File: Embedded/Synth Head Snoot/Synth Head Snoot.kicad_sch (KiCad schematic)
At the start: 0 parts

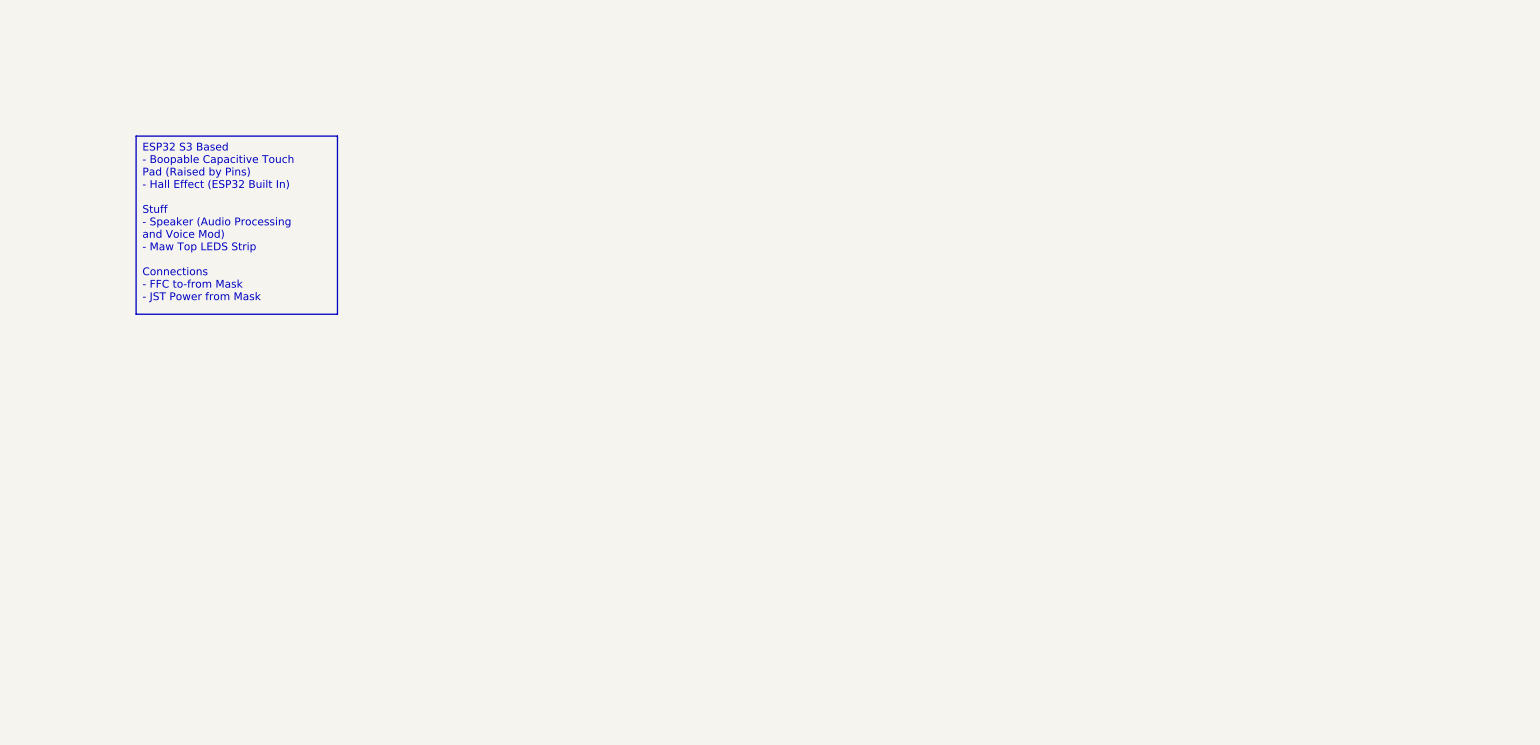
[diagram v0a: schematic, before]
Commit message: Majority of the pins for the Mask Board & Snoot Added
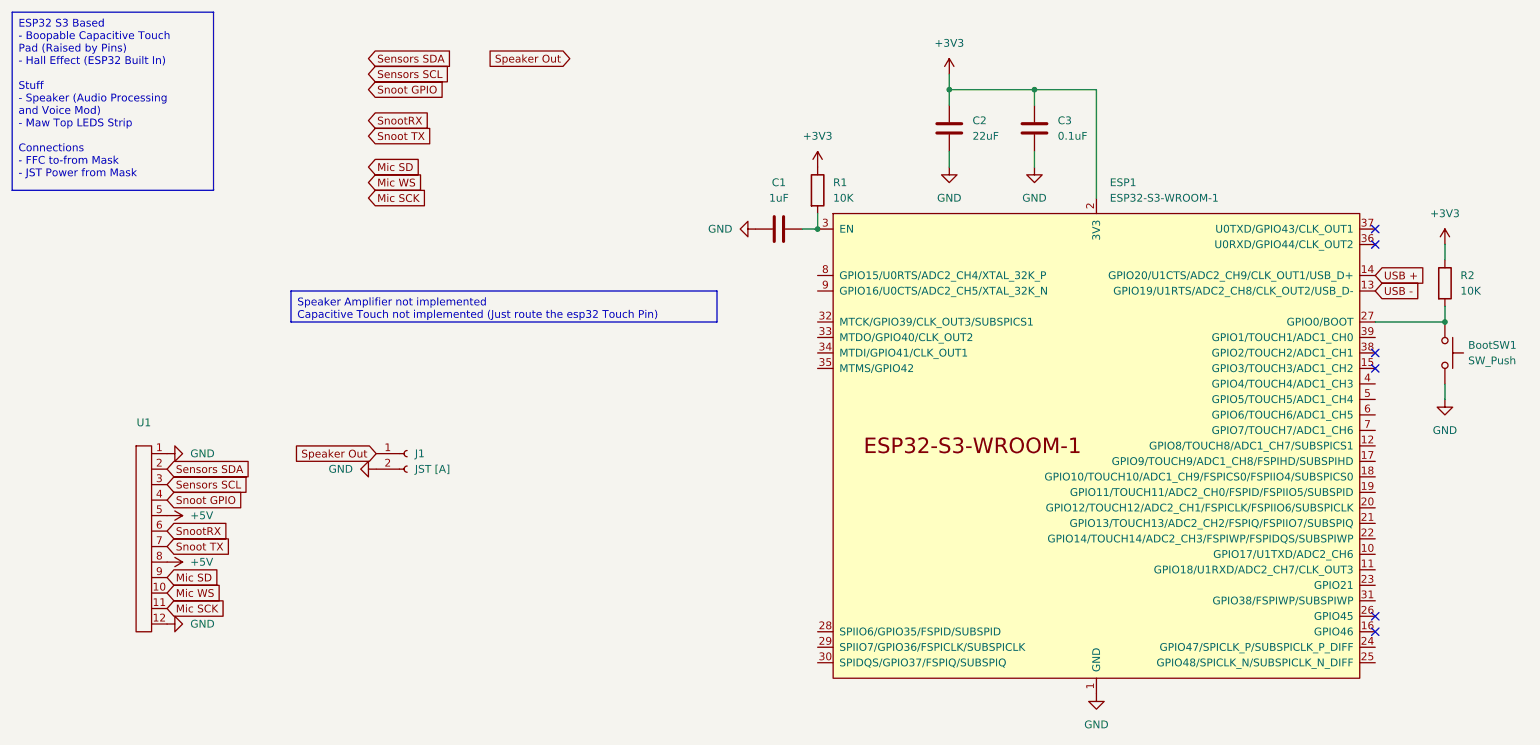
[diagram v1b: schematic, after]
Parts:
- added BootSW1: SW_Push, Button-R-667843:Button-R-667843, symbol Switch:SW_Push
- added C1: 1uF, Capacitor_SMD:C_0603_1608Metric, symbol Device:C
- added C2: 22uF, Capacitor_SMD:C_0603_1608Metric_Pad1.08x0.95mm_HandSolder, symbol Device:C
- added C3: 0.1uF, Capacitor_SMD:C_0603_1608Metric, symbol Device:C
- added ESP1: ESP32-S3-WROOM-1, PCM_Espressif:ESP32-S3-WROOM-1U, symbol PCM_Espressif:ESP32-S3-WROOM-1
- added J1: JST [A], symbol Connector:Conn_01x02_Socket
- added R1, R2: 10K, Resistor_SMD:R_0603_1608Metric, symbol Device:R
- added U1: ~, symbol FCC_Connector:FFC_12P
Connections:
- new net: C1.2, ESP1.3 (EN), R1.2
- new net: BootSW1.1, ESP1.27 (GPIO0/BOOT), R2.2
- new net +3V3: C2.1, C3.1, ESP1.2 (3V3), R1.1, R2.1
- new net +5V: U1.5, U1.8
- new net GND: BootSW1.2, C1.1, C2.2, C3.2, ESP1.1 (GND), ESP1.40 (GND), ESP1.41 (GND), J1.2 (Pin_2), U1.1, U1.12
- new net Mic SCK: U1.11
- new net Mic SD: U1.9
- new net Mic WS: U1.10
- new net Sensors SCL: U1.3
- new net Sensors SDA: U1.2
- new net Snoot GPIO: U1.4
- new net Snoot TX: U1.7
- new net SnootRX: U1.6
- new net Speaker Out: J1.1 (Pin_1)
- new net USB +: ESP1.14 (GPIO20/U1CTS/ADC2_CH9/CLK_OUT1/USB_D+)
- new net USB -: ESP1.13 (GPIO19/U1RTS/ADC2_CH8/CLK_OUT2/USB_D-)
- no-connect marks 0 -> 6

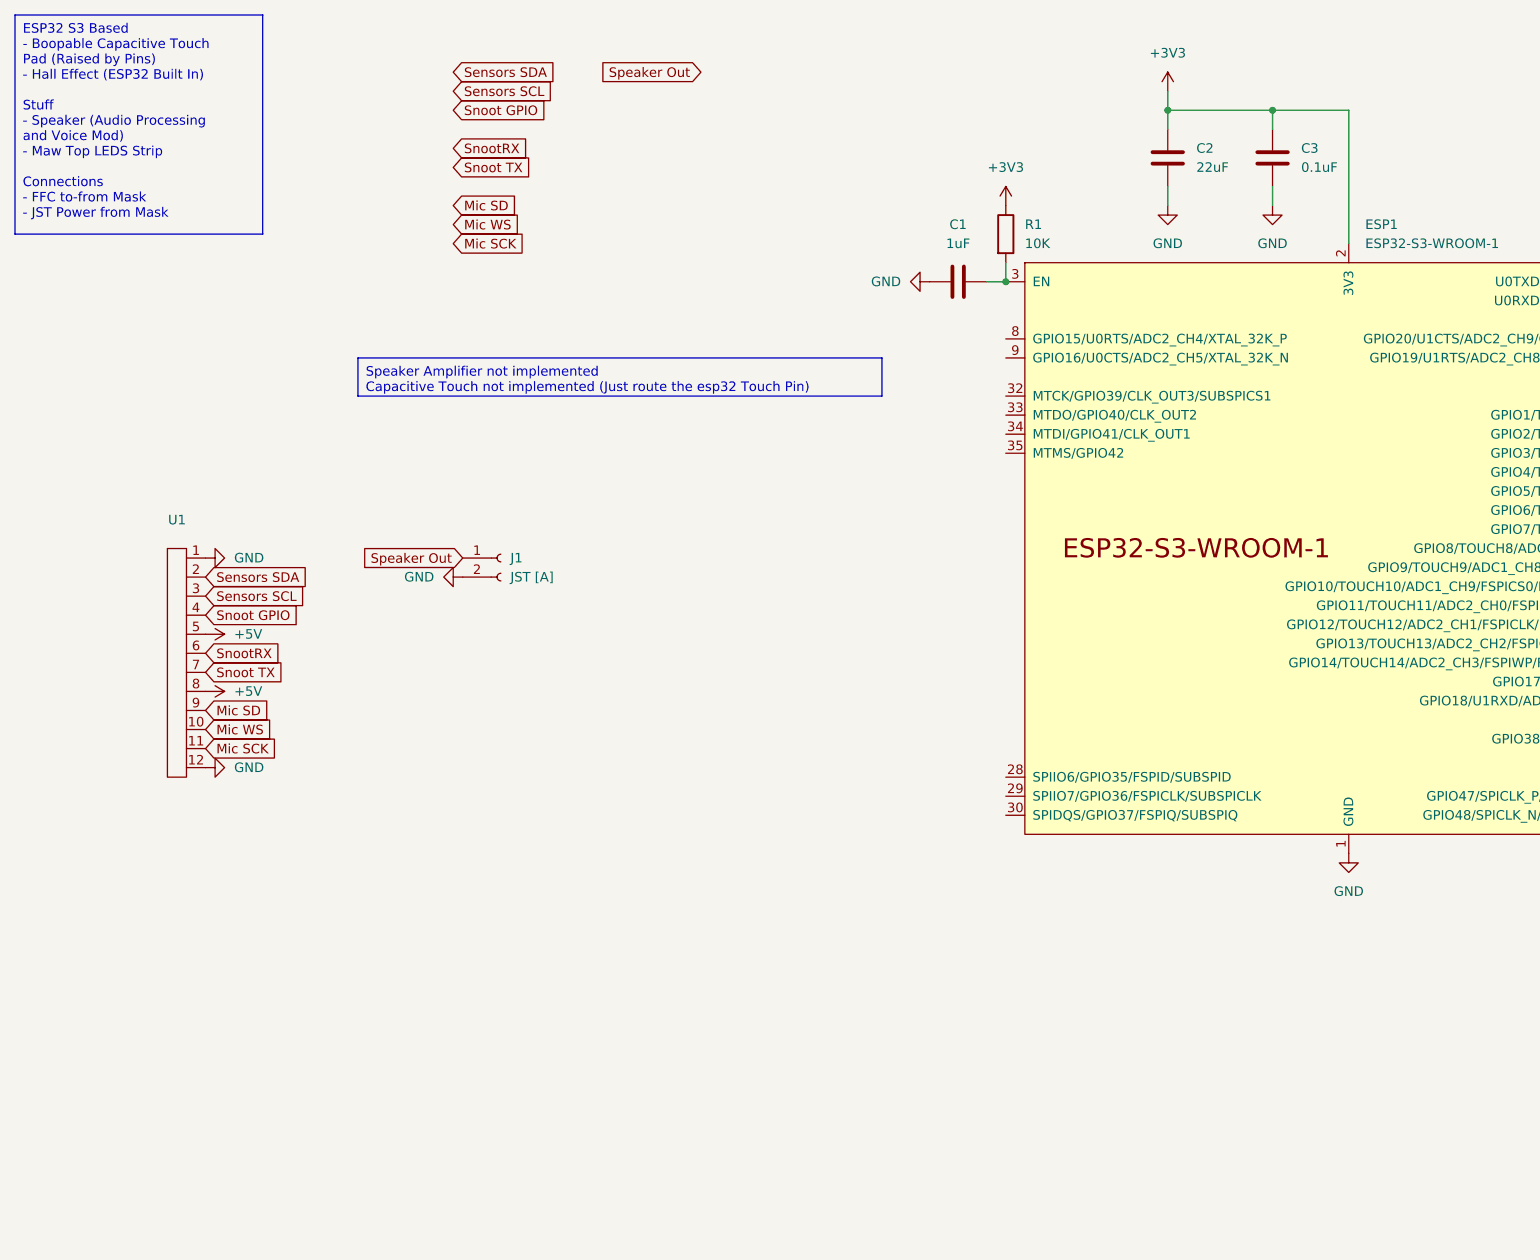
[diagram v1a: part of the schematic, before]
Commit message: Added Speaker, Power & USB C to Snoot Board
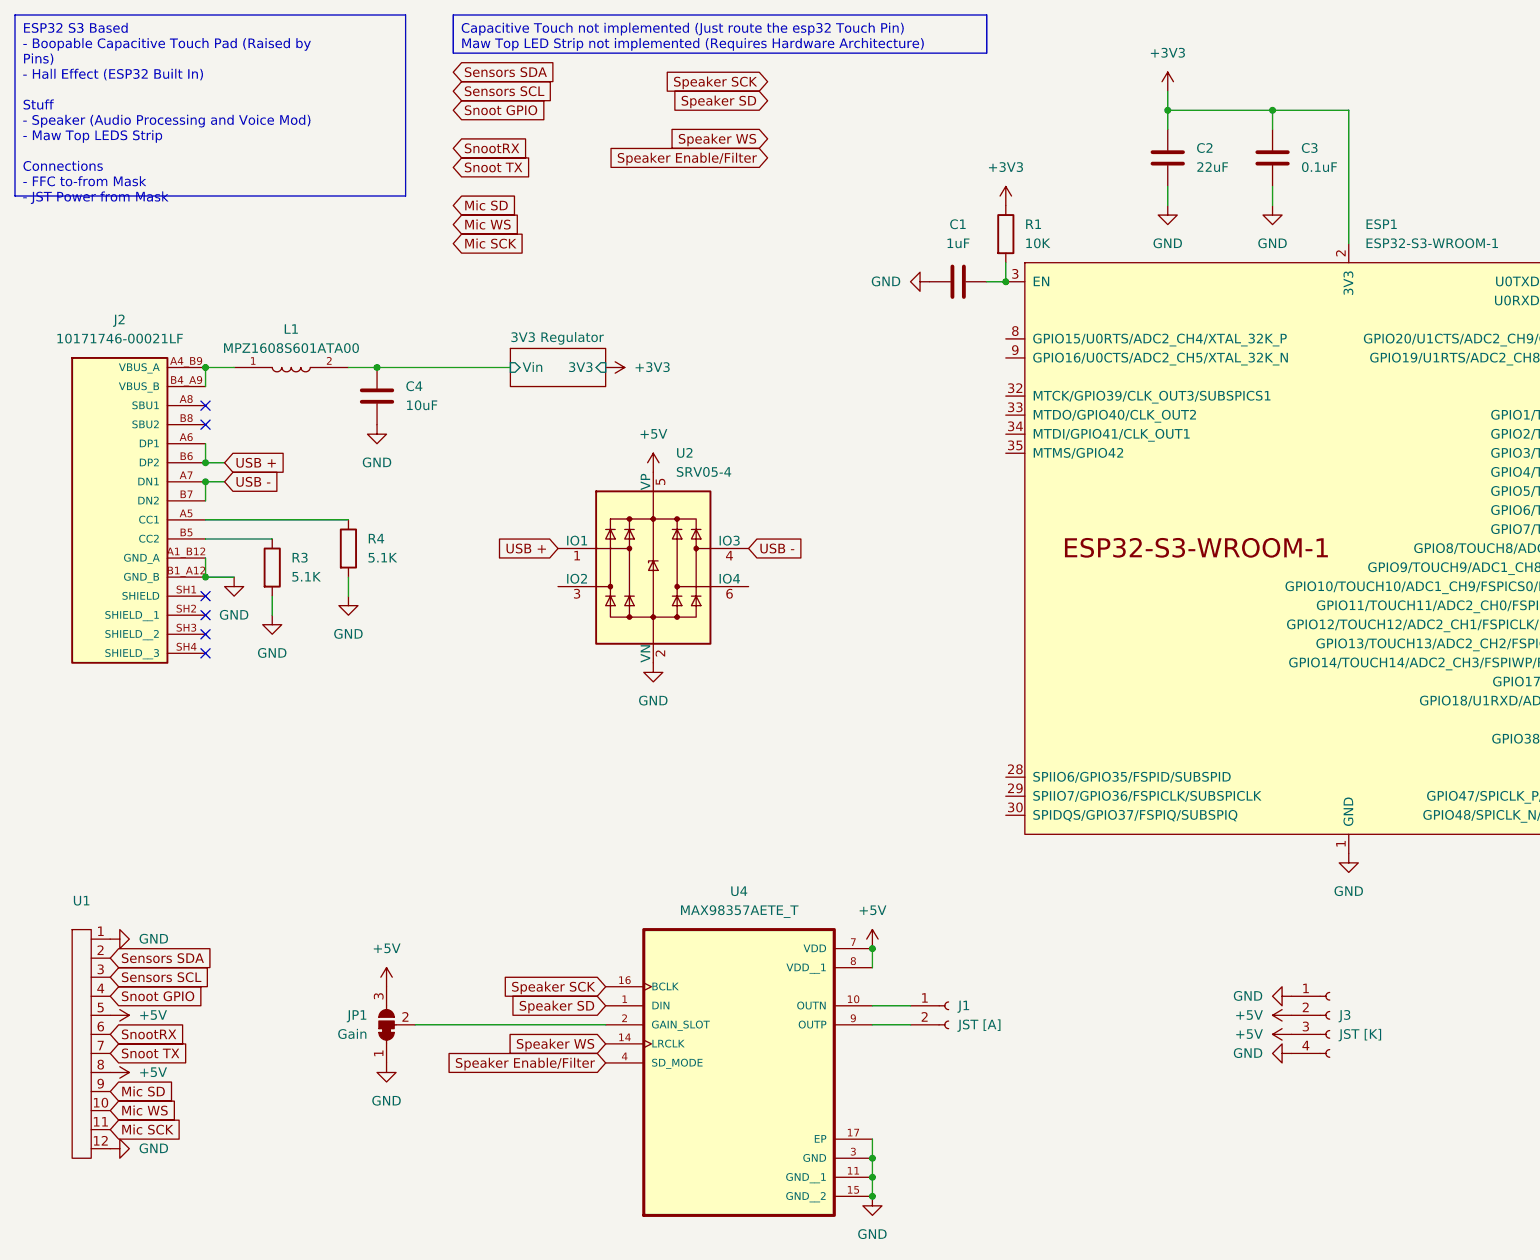
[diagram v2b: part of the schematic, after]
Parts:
- added C4: 10uF, Capacitor_SMD:C_0603_1608Metric, symbol Device:C
- added J2: 10171746-00021LF, USBC_10171746_00021LF:AMPHENOL_10171746-00021LF, symbol USBC_10171746_00021LF:10171746-00021LF
- added J3: JST [K], symbol Connector:Conn_01x04_Socket
- added JP1: Gain, symbol Jumper:SolderJumper_3_Bridged12
- added L1: MPZ1608S601ATA00, Ferrite_Bead_MPZ1608S601ATA00:INDC1608X95N, symbol Ferrite_Bead_MPZ1608S601ATA00:MPZ1608S601ATA00
- added R3, R4: 5.1K, Resistor_SMD:R_0603_1608Metric, symbol Device:R
- added U2: SRV05-4, Package_TO_SOT_SMD:SOT-23-6, symbol Power_Protection:SRV05-4
- added U4: MAX98357AETE_T, MAX98357AETE_T:QFN50P300X300X80-17N, symbol I2S_Audio_MAX98357A:MAX98357AETE_T
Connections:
- net +5V: now also J3.2 (Pin_2), J3.3 (Pin_3), JP1.3 (B), U2.5 (VP), U4.7 (VDD), U4.8 (VDD__1)
- net GND: now also C4.2, J2.A1_B12 (GND_A), J2.B1_A12 (GND_B), J3.1 (Pin_1), J3.4 (Pin_4), JP1.1 (A), R3.2, R4.2, U2.2 (VN), U4.11 (GND__1), U4.15 (GND__2), U4.17 (EP), U4.3 (GND); no longer J1.2 (Pin_2)
- net USB +: now also J2.A6 (DP1), J2.B6 (DP2), U2.1 (IO1)
- net USB -: now also J2.A7 (DN1), J2.B7 (DN2), U2.4 (IO3)
- net Speaker Out: no longer names the net of J1.1 (Pin_1)
- net Speaker Out: now also U4.10 (OUTN)
- new net: J1.2 (Pin_2), U4.9 (OUTP)
- new net: JP1.2 (C), U4.2 (GAIN_SLOT)
- new net: J2.B5 (CC2), R3.1
- new net: J2.A4_B9 (VBUS_A), J2.B4_A9 (VBUS_B), L1.1
- new net: J2.A5 (CC1), R4.1
- new net 3V3 Regulator/Vin: C4.1, L1.2
- new net Speaker Enable/Filter: U4.4 (SD_MODE)
- new net Speaker SCK: U4.16 (BCLK)
- new net Speaker SD: U4.1 (DIN)
- new net Speaker WS: U4.14 (LRCLK)
- no-connect marks 6 -> 12
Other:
- added sheet 3V3 Regulator (3V3 Reg.kicad_sch)
- moved on the sheet: J1, U1

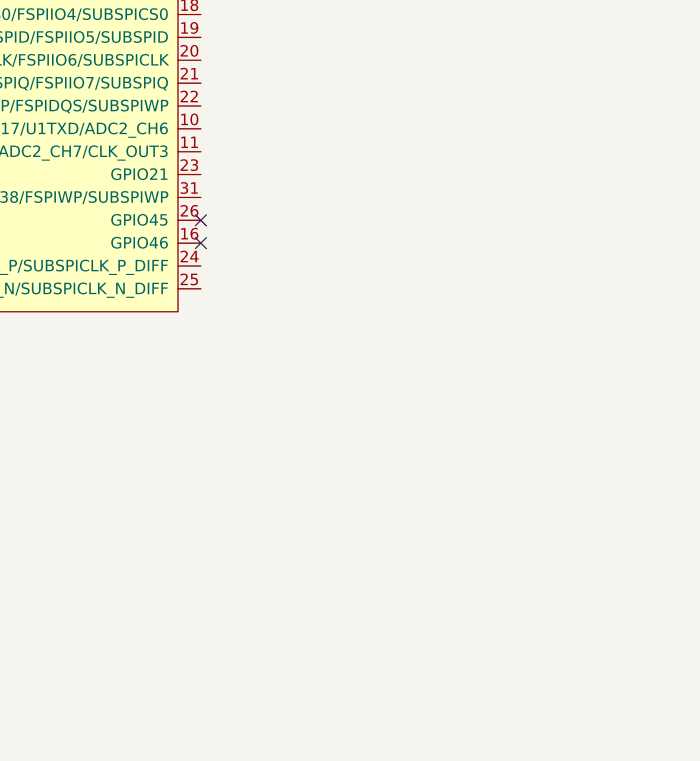
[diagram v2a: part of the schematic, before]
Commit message: Nearly completed Mask Board
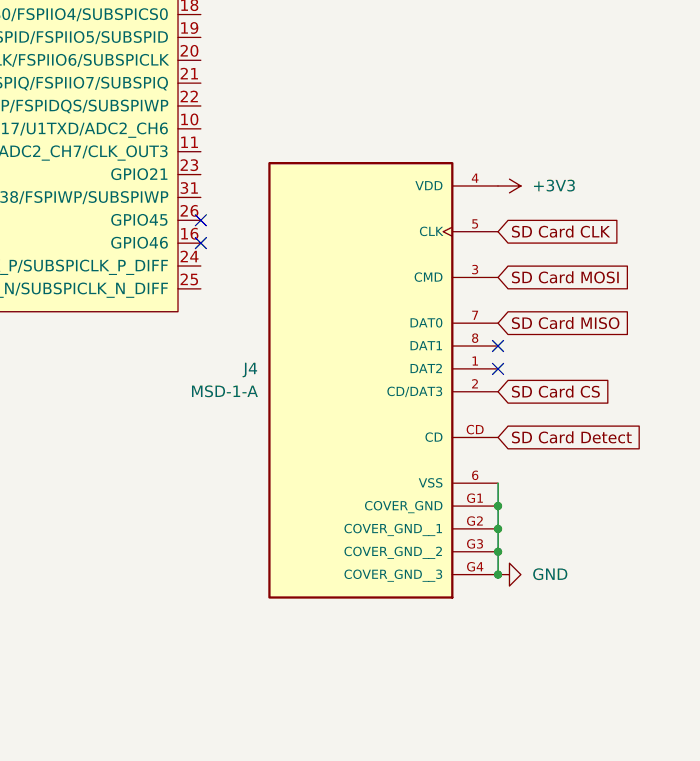
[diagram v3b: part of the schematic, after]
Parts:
- added J4: MSD-1-A, MSD-1-A:CUI_MSD-1-A, symbol MicroSD_MSD_1_A:MSD-1-A
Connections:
- net +3V3: now also J4.4 (VDD)
- net GND: now also J4.6 (VSS), J4.G1 (COVER_GND), J4.G2 (COVER_GND__1), J4.G3 (COVER_GND__2), J4.G4 (COVER_GND__3)
- new net SD Card CLK: J4.5 (CLK)
- new net SD Card CS: J4.2 (CD/DAT3)
- new net SD Card Detect: J4.CD
- new net SD Card MISO: J4.7 (DAT0)
- new net SD Card MOSI: J4.3 (CMD)
- no-connect marks 12 -> 14
